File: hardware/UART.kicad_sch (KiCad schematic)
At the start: 9 parts

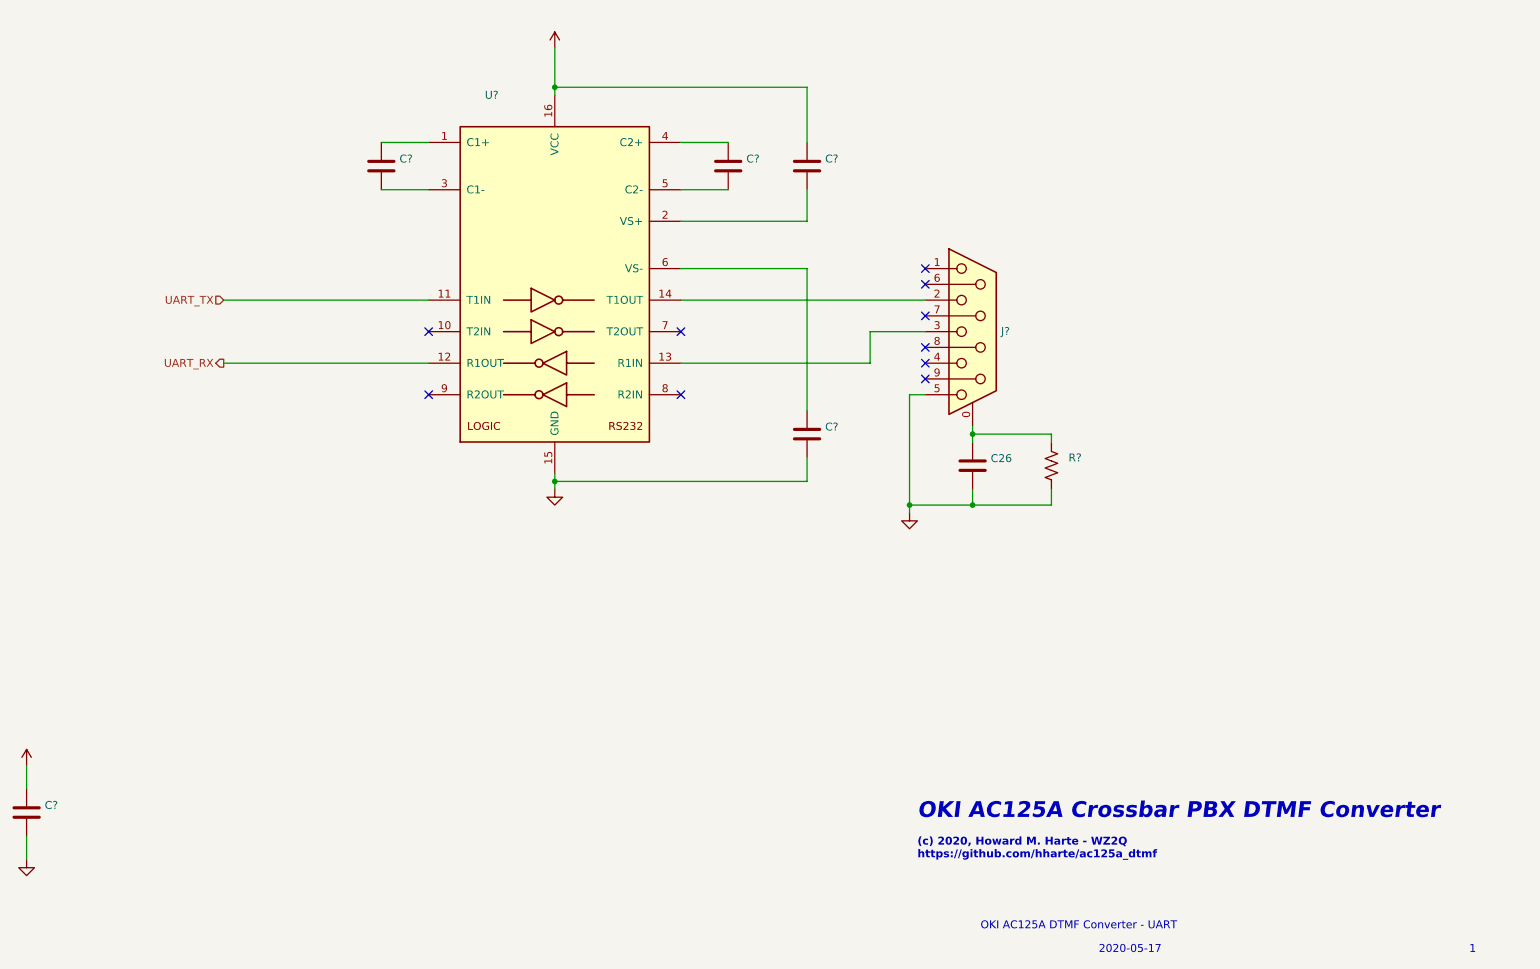
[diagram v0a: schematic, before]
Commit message: Fix a couple DRC errors in the layout.
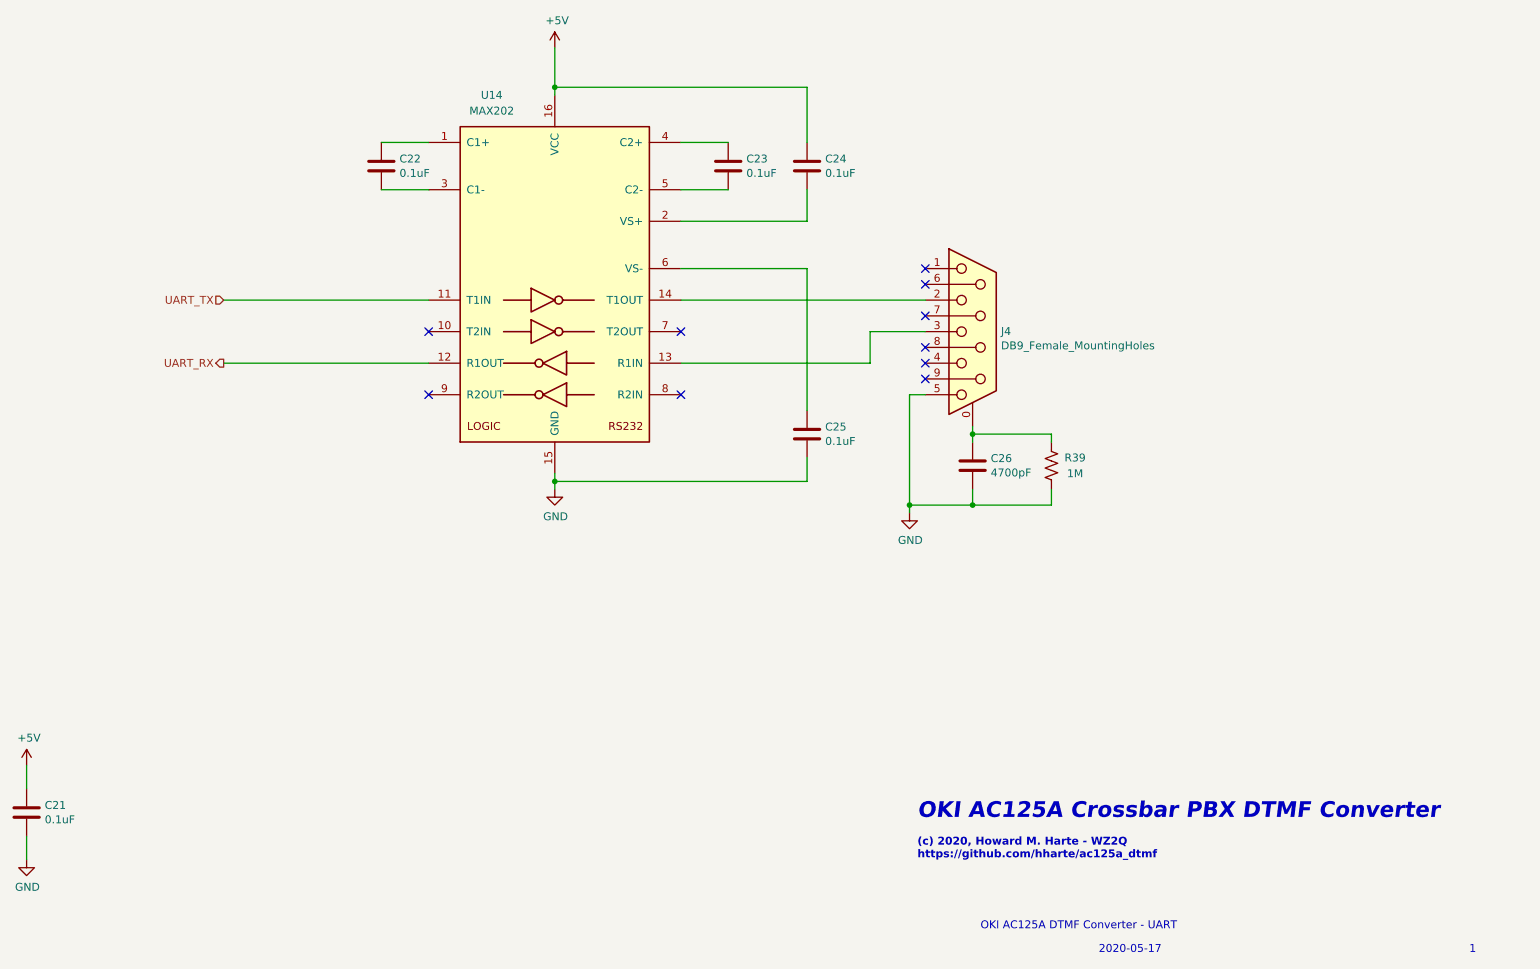
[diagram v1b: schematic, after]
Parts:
- C21, C22, C23, C24, C25: renamed from C?; value (none) -> 0.1uF; footprint (none) -> Capacitor_THT:C_Disc_D3.0mm_W2.0mm_P2.50mm
- C26: value (none) -> 4700pF; footprint (none) -> Capacitor_THT:C_Disc_D4.3mm_W1.9mm_P5.00mm
- J4: renamed from J?; value (none) -> DB9_Female_MountingHoles; footprint (none) -> Connector_Dsub:DSUB-9_Female_Horizontal_P2.77x2.84mm_EdgePinOffset7.70mm_Housed_MountingHolesOffset9.12mm
- R39: renamed from R?; value (none) -> 1M; footprint (none) -> Resistor_THT:R_Axial_DIN0207_L6.3mm_D2.5mm_P7.62mm_Horizontal
- U14: renamed from U?; value (none) -> MAX202; footprint (none) -> Package_DIP:DIP-16_W7.62mm
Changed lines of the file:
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@@
   (symbol (lib_id "Connector:DB9_Female_MountingHoles") (at 189.23 93.98 0) (unit 1)
     (in_bom yes) (on_board yes)
-    (property "Reference" "J?" (id 0) (at 193.802 93.9292 0)
-      (effects (font (size 1.27 1.27)) (justify left))
-    )
-    (property "Value" "" (id 1) (at 193.802 96.2406 0)
-      (effects (font (size 1.27 1.27)) (justify left))
-    )
-    (property "Footprint" "" (id 2) (at 189.23 93.98 0)
+    (property "Reference" "J4" (id 0) (at 193.802 93.9292 0)
+      (effects (font (size 1.27 1.27)) (justify left))
+    )
+    (property "Value" "DB9_Female_MountingHoles" (id 1) (at 193.802 96.2406 0)
+      (effects (font (size 1.27 1.27)) (justify left))
+    )
+    (property "Footprint" "Connector_Dsub:DSUB-9_Female_Horizontal_P2.77x2.84mm_EdgePinOffset7.70mm_Housed_MountingHolesOffset9.12mm" (id 2) (at 189.23 93.98 0)
       (effects (font (size 1.27 1.27)) hide)
     )
@@
   (symbol (lib_id "Interface_UART:MAX202") (at 121.92 86.36 0) (unit 1)
     (in_bom yes) (on_board yes)
-    (property "Reference" "U?" (id 0) (at 111.76 55.88 0))
-    (property "Value" "" (id 1) (at 111.76 58.42 0))
-    (property "Footprint" "" (id 2) (at 123.19 113.03 0)
+    (property "Reference" "U14" (id 0) (at 111.76 55.88 0))
+    (property "Value" "MAX202" (id 1) (at 111.76 58.42 0))
+    (property "Footprint" "Package_DIP:DIP-16_W7.62mm" (id 2) (at 123.19 113.03 0)
       (effects (font (size 1.27 1.27)) (justify left) hide)
     )
@@
   (symbol (lib_id "power:GND") (at 121.92 119.38 0) (unit 1)
     (in_bom yes) (on_board yes)
-    (property "Reference" "#PWR?" (id 0) (at 121.92 125.73 0)
-      (effects (font (size 1.27 1.27)) hide)
-    )
-    (property "Value" "" (id 1) (at 122.047 123.7742 0))
+    (property "Reference" "#PWR0111" (id 0) (at 121.92 125.73 0)
+      (effects (font (size 1.27 1.27)) hide)
+    )
+    (property "Value" "GND" (id 1) (at 122.047 123.7742 0))
     (property "Footprint" "" (id 2) (at 121.92 119.38 0)
       (effects (font (size 1.27 1.27)) hide)
@@
   (symbol (lib_id "power:+5V") (at 121.92 48.26 0) (unit 1)
     (in_bom yes) (on_board yes)
-    (property "Reference" "#PWR?" (id 0) (at 121.92 52.07 0)
-      (effects (font (size 1.27 1.27)) hide)
-    )
-    (property "Value" "" (id 1) (at 122.301 43.8658 0))
+    (property "Reference" "#PWR0112" (id 0) (at 121.92 52.07 0)
+      (effects (font (size 1.27 1.27)) hide)
+    )
+    (property "Value" "+5V" (id 1) (at 122.301 43.8658 0))
     (property "Footprint" "" (id 2) (at 121.92 48.26 0)
       (effects (font (size 1.27 1.27)) hide)
@@
   (symbol (lib_id "power:GND") (at 179.07 123.19 0) (unit 1)
     (in_bom yes) (on_board yes)
-    (property "Reference" "#PWR?" (id 0) (at 179.07 129.54 0)
-      (effects (font (size 1.27 1.27)) hide)
-    )
-    (property "Value" "" (id 1) (at 179.197 127.5842 0))
+    (property "Reference" "#PWR0117" (id 0) (at 179.07 129.54 0)
+      (effects (font (size 1.27 1.27)) hide)
+    )
+    (property "Value" "GND" (id 1) (at 179.197 127.5842 0))
     (property "Footprint" "" (id 2) (at 179.07 123.19 0)
       (effects (font (size 1.27 1.27)) hide)
@@
   (symbol (lib_id "power:+5V") (at 36.83 163.83 0) (unit 1)
     (in_bom yes) (on_board yes)
-    (property "Reference" "#PWR?" (id 0) (at 36.83 167.64 0)
-      (effects (font (size 1.27 1.27)) hide)
-    )
-    (property "Value" "" (id 1) (at 37.211 159.4358 0))
+    (property "Reference" "#PWR0113" (id 0) (at 36.83 167.64 0)
+      (effects (font (size 1.27 1.27)) hide)
+    )
+    (property "Value" "+5V" (id 1) (at 37.211 159.4358 0))
     (property "Footprint" "" (id 2) (at 36.83 163.83 0)
       (effects (font (size 1.27 1.27)) hide)
@@
   (symbol (lib_id "Device:C") (at 36.83 171.45 0) (unit 1)
     (in_bom yes) (on_board yes)
-    (property "Reference" "C?" (id 0) (at 39.751 170.2816 0)
-      (effects (font (size 1.27 1.27)) (justify left))
-    )
-    (property "Value" "" (id 1) (at 39.751 172.593 0)
-      (effects (font (size 1.27 1.27)) (justify left))
-    )
-    (property "Footprint" "" (id 2) (at 37.7952 175.26 0)
+    (property "Reference" "C21" (id 0) (at 39.751 170.2816 0)
+      (effects (font (size 1.27 1.27)) (justify left))
+    )
+    (property "Value" "0.1uF" (id 1) (at 39.751 172.593 0)
+      (effects (font (size 1.27 1.27)) (justify left))
+    )
+    (property "Footprint" "Capacitor_THT:C_Disc_D3.0mm_W2.0mm_P2.50mm" (id 2) (at 37.7952 175.26 0)
       (effects (font (size 1.27 1.27)) hide)
     )
@@
   (symbol (lib_id "power:GND") (at 36.83 179.07 0) (unit 1)
     (in_bom yes) (on_board yes)
-    (property "Reference" "#PWR?" (id 0) (at 36.83 185.42 0)
-      (effects (font (size 1.27 1.27)) hide)
-    )
-    (property "Value" "" (id 1) (at 36.957 183.4642 0))
+    (property "Reference" "#PWR0116" (id 0) (at 36.83 185.42 0)
+      (effects (font (size 1.27 1.27)) hide)
+    )
+    (property "Value" "GND" (id 1) (at 36.957 183.4642 0))
     (property "Footprint" "" (id 2) (at 36.83 179.07 0)
       (effects (font (size 1.27 1.27)) hide)
@@
   (symbol (lib_id "Device:C") (at 149.86 67.31 0) (unit 1)
     (in_bom yes) (on_board yes)
-    (property "Reference" "C?" (id 0) (at 152.781 66.1416 0)
-      (effects (font (size 1.27 1.27)) (justify left))
-    )
-    (property "Value" "" (id 1) (at 152.781 68.453 0)
-      (effects (font (size 1.27 1.27)) (justify left))
-    )
-    (property "Footprint" "" (id 2) (at 150.8252 71.12 0)
+    (property "Reference" "C23" (id 0) (at 152.781 66.1416 0)
+      (effects (font (size 1.27 1.27)) (justify left))
+    )
+    (property "Value" "0.1uF" (id 1) (at 152.781 68.453 0)
+      (effects (font (size 1.27 1.27)) (justify left))
+    )
+    (property "Footprint" "Capacitor_THT:C_Disc_D3.0mm_W2.0mm_P2.50mm" (id 2) (at 150.8252 71.12 0)
       (effects (font (size 1.27 1.27)) hide)
     )
@@
   (symbol (lib_id "Device:C") (at 93.98 67.31 0) (unit 1)
     (in_bom yes) (on_board yes)
-    (property "Reference" "C?" (id 0) (at 96.901 66.1416 0)
-      (effects (font (size 1.27 1.27)) (justify left))
-    )
-    (property "Value" "" (id 1) (at 96.901 68.453 0)
-      (effects (font (size 1.27 1.27)) (justify left))
-    )
-    (property "Footprint" "" (id 2) (at 94.9452 71.12 0)
+    (property "Reference" "C22" (id 0) (at 96.901 66.1416 0)
+      (effects (font (size 1.27 1.27)) (justify left))
+    )
+    (property "Value" "0.1uF" (id 1) (at 96.901 68.453 0)
+      (effects (font (size 1.27 1.27)) (justify left))
+    )
+    (property "Footprint" "Capacitor_THT:C_Disc_D3.0mm_W2.0mm_P2.50mm" (id 2) (at 94.9452 71.12 0)
       (effects (font (size 1.27 1.27)) hide)
     )
@@
   (symbol (lib_id "Device:C") (at 162.56 67.31 0) (unit 1)
     (in_bom yes) (on_board yes)
-    (property "Reference" "C?" (id 0) (at 165.481 66.1416 0)
-      (effects (font (size 1.27 1.27)) (justify left))
-    )
-    (property "Value" "" (id 1) (at 165.481 68.453 0)
-      (effects (font (size 1.27 1.27)) (justify left))
-    )
-    (property "Footprint" "" (id 2) (at 163.5252 71.12 0)
+    (property "Reference" "C24" (id 0) (at 165.481 66.1416 0)
+      (effects (font (size 1.27 1.27)) (justify left))
+    )
+    (property "Value" "0.1uF" (id 1) (at 165.481 68.453 0)
+      (effects (font (size 1.27 1.27)) (justify left))
+    )
+    (property "Footprint" "Capacitor_THT:C_Disc_D3.0mm_W2.0mm_P2.50mm" (id 2) (at 163.5252 71.12 0)
       (effects (font (size 1.27 1.27)) hide)
     )
@@
   (symbol (lib_id "Device:C") (at 162.56 110.49 0) (unit 1)
     (in_bom yes) (on_board yes)
-    (property "Reference" "C?" (id 0) (at 165.481 109.3216 0)
-      (effects (font (size 1.27 1.27)) (justify left))
-    )
-    (property "Value" "" (id 1) (at 165.481 111.633 0)
-      (effects (font (size 1.27 1.27)) (justify left))
-    )
-    (property "Footprint" "" (id 2) (at 163.5252 114.3 0)
+    (property "Reference" "C25" (id 0) (at 165.481 109.3216 0)
+      (effects (font (size 1.27 1.27)) (justify left))
+    )
+    (property "Value" "0.1uF" (id 1) (at 165.481 111.633 0)
+      (effects (font (size 1.27 1.27)) (justify left))
+    )
+    (property "Footprint" "Capacitor_THT:C_Disc_D3.0mm_W2.0mm_P2.50mm" (id 2) (at 163.5252 114.3 0)
       (effects (font (size 1.27 1.27)) hide)
     )
@@
       (effects (font (size 1.27 1.27)) (justify left))
     )
-    (property "Value" "" (id 1) (at 192.151 116.713 0)
-      (effects (font (size 1.27 1.27)) (justify left))
-    )
-    (property "Footprint" "" (id 2) (at 190.1952 119.38 0)
+    (property "Value" "4700pF" (id 1) (at 192.151 116.713 0)
+      (effects (font (size 1.27 1.27)) (justify left))
+    )
+    (property "Footprint" "Capacitor_THT:C_Disc_D4.3mm_W1.9mm_P5.00mm" (id 2) (at 190.1952 119.38 0)
       (effects (font (size 1.27 1.27)) hide)
     )
@@
   (symbol (lib_id "Device:R_US") (at 201.93 115.57 0) (unit 1)
     (in_bom yes) (on_board yes)
-    (property "Reference" "R?" (id 0) (at 205.74 114.3 0))
-    (property "Value" "" (id 1) (at 205.74 116.84 0))
-    (property "Footprint" "" (id 2) (at 202.946 115.824 90)
-      (effects (font (size 1.27 1.27)) hide)
-    )
+    (property "Reference" "R39" (id 0) (at 205.74 114.3 0))
+    (property "Value" "1M" (id 1) (at 205.74 116.84 0))
+    (property "Footprint" "Resistor_THT:R_Axial_DIN0207_L6.3mm_D2.5mm_P7.62mm_Horizontal" (id 2) (at 202.946 115.824 90)
+      (effects (font (size 1.27 1.27)) hide)
+    )
